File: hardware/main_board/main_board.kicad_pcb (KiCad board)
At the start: 4 copper layers, 155.2 x 50 mm, 179 parts, among them J1 USB_C_Receptacle_USB2.0_16P, J2 BAT1, J3 Conn_02x05_Odd_Even, J4 Conn_02x05_Odd_Even, Q1 FDMC4435BZ, Q10 MMBTA92, Q11 MMBTA92, Q12 MMBTA42, Q13 MMBTA42, Q14 MMBTA92, Q15 MMBTA92, Q16 MMBTA42, Q17 MMBTA42, Q18 MMBTA92, Q19 MMBTA92, Q2 MMBT3904, Q20 FDS2734, Q3 MMBT3904, Q4 MMBTA42, Q5 MMBTA42, Q6 MMBTA92, Q7 MMBTA92, Q8 MMBTA42, Q9 MMBTA42, SW1 PTS645VK31LFS, SW2 PTS645VK31LFS, SW3 PTS645VK31LFS, U1 SRV05-4, U10 TPS61022, U11 ESP32-S3-WROOM1, U12 TPS2121, U13 TPS22810DBVR, U14 74HC238, U15 LM5155, U16 BQ27441DRZR-G1A, U2 CP2102N-A02-GQFN28, U3 HUSB238_002DD, U4 TPS22918DBVR, U5 BQ25601, U6 DFPlayer_mini, U7 DS3231MZ, U8 TPS63802, U9 NCH2800HV

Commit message: WIP: update mainboard componemt LCSC PN
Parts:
- C28: value 120n -> 220n
- C29: value 50p -> 220p
- J2, LS1: footprint Connector_JST:JST_XH_S2B-XH-A_1x02_P2.50mm_Horizontal -> Connector_JST:JST_PH_B2B-PH-SM4-TB_1x02-1MP_P2.00mm_Vertical
- R74: value 22k -> 3.3k
- moved LS1 2.93 mm to (82.7, 125.9), turned to 0 degrees
- moved J2 2.02 mm to (193.7, 141.0), turned to 90 degrees
- moved C7 1.79 mm to (91.2, 129.8)
- moved C4 1.79 mm to (94.0, 124.4)
- moved U4 1.79 mm to (94.2, 129.9)
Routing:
- net DF_EN: track 5.15 -> 55.7 mm
- net Net-(U6-SPK_2): track 33.2 -> 28.5 mm
- net +5V: track 161.6 -> 159.1 mm
- net Net-(U6-SPK_1): track 21.3 -> 23.4 mm
- net Net-(U4-VOUT): track 20.3 -> 21.2 mm
- net VBAT: track 170.2 -> 169.3 mm, vias 4 -> 5
- net U1RXD: track 64.8 -> 64.1 mm

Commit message: WIP: mainboard schematic
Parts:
- moved J2 1.07 mm to (192.6, 141.2)
- moved C7 0.56 mm to (90.6, 129.7)
- moved C4 0.56 mm to (93.5, 124.2)
- moved U4 0.56 mm to (93.7, 129.8)
- moved LS1 0.50 mm to (83.1, 126.2)
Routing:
- net I2C0_SCL: track 104.3 -> 168.7 mm
- net I2C1_SDA: track 41.1 -> 76.6 mm
- net I2C1_SCL: track 40.0 -> 73.8 mm
- net I2C0_SDA: track 139.7 -> 171.6 mm
- net CHIP_PU: track 13.7 -> 37.0 mm, vias 1 -> 2
- net Net-(U13-VIN): track 10.3 -> 17.0 mm, vias 0 -> 1
- net VSYS: track 33.5 -> 39.8 mm
- net +5V: track 159.1 -> 164.7 mm
- net GND: track 89.0 -> 93.1 mm
- net DF_EN: track 55.7 -> 59.7 mm
- net BAT_LOW: track 88.2 -> 84.3 mm
- net +3V3: track 164.9 -> 162.5 mm, vias 5 -> 8
- net PGND1: track 24.5 -> 22.1 mm, vias 34 -> 37
- net Net-(Q12-B): track 0.00 -> 1.71 mm
- net VBAT: track 169.3 -> 167.8 mm
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
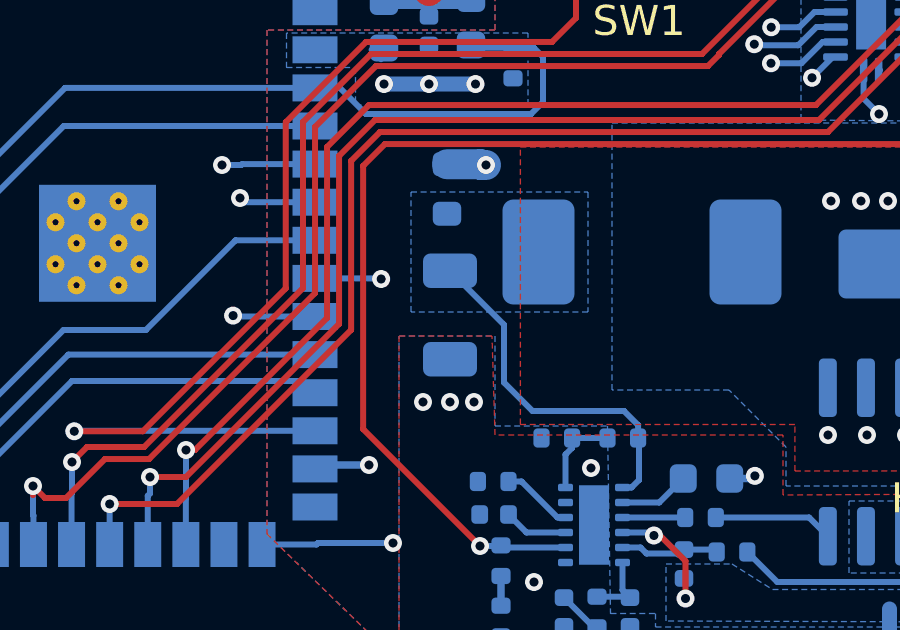
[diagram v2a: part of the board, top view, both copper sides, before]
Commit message: hw(main_board): update LCSC PN
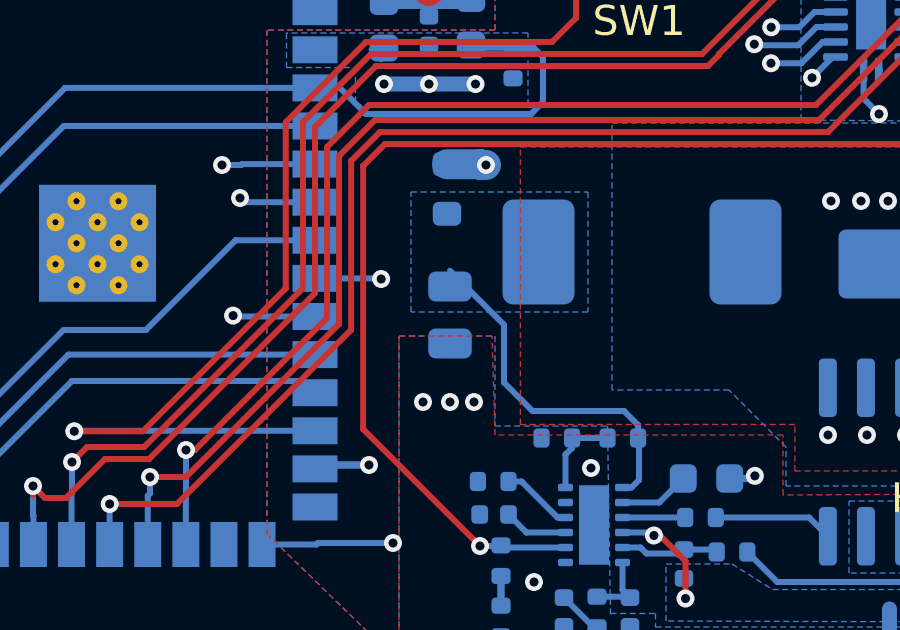
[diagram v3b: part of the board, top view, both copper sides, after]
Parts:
- C22: value 100nF -> 100n
- C25: value 100u -> 10u; footprint Capacitor_SMD:C_1206_3216Metric -> Capacitor_SMD:C_0805_2012Metric

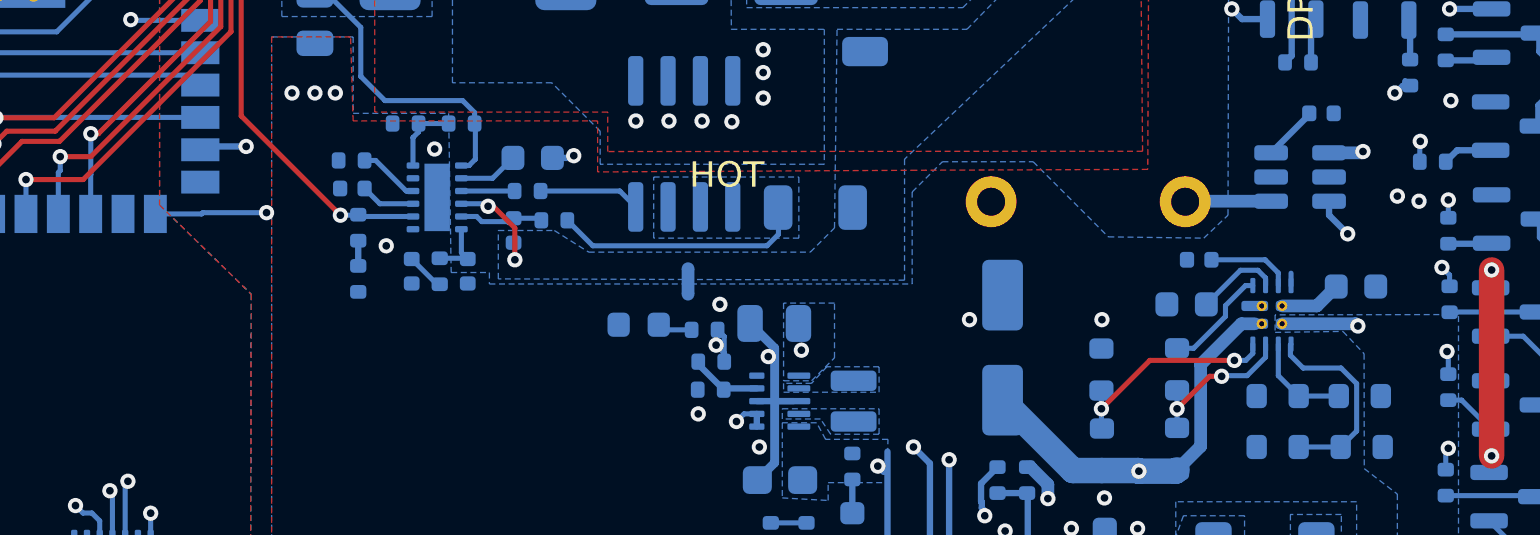
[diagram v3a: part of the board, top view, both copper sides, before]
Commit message: hw(sch): add input detect signal from TPS2121 to let ESP32 know which input is selected for HV power
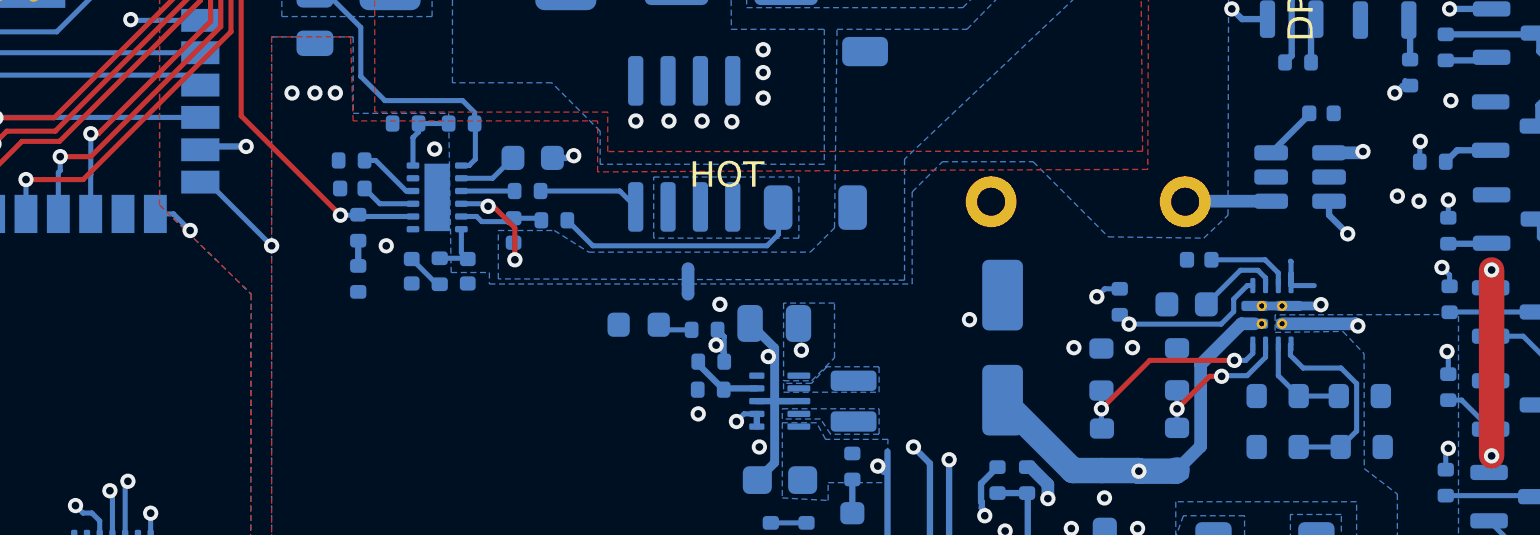
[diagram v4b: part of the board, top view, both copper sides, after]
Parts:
- removed C21: 1u, Capacitor_SMD:C_0603_1608Metric
- added R84: 10k, Resistor_SMD:R_0402_1005Metric, B.Cu at (171.3, 124.9)
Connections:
- U11 pad 14: unconnected-(U11-IO20-Pad14) -> VIN_ST
- U12 pad 9: PGND1 -> VIN_ST
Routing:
- net VIN_ST: track 0.00 -> 45.1 mm, vias 0 -> 2
- net +5V: track 164.7 -> 175.8 mm, vias 7 -> 8
- net PGND1: track 22.1 -> 19.7 mm, vias 37 -> 38
- net Net-(U13-VIN): track 17.0 -> 15.5 mm, vias 1 -> 2

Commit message: layout(main): adjust layout
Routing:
- net +5V: track 175.8 -> 174.5 mm
- net Net-(D4-A): vias 11 -> 23
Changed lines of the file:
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@@
 		(tags "RUX0012A Texas VQFN-HR NoLead")
 		(property "Reference" "U12"
-			(at -0.025 2.4125 0)
+			(at -3.225 1.4125 0)
 			(layer "B.SilkS")
 			(effects
@@
 		(tags "resistor")
 		(property "Reference" "R82"
-			(at 0.41 1.3 90)
+			(at 0.71 1.4 90)
 			(layer "B.SilkS")
 			(effects
@@
 		(tags "resistor")
 		(property "Reference" "R83"
-			(at 1.2 1.2 90)
+			(at 1.6 1.4 90)
 			(layer "B.SilkS")
 			(effects
@@
 		(tags "capacitor")
 		(property "Reference" "R36"
-			(at 2.95 0 0)
+			(at 1.925 1.8 0)
 			(layer "B.SilkS")
 			(effects
@@
 		(tags "capacitor")
 		(property "Reference" "C22"
-			(at 2.8 0.15 0)
+			(at -2.78 0.65 0)
 			(layer "B.SilkS")
 			(effects
@@
 		(tags "resistor")
 		(property "Reference" "R84"
-			(at 0 1.17 90)
+			(at 1.7 -2.1 0)
 			(layer "B.SilkS")
 			(effects
@@
 	)
 	(via
-		(at 97.425 124.375)
+		(at 98.2 124.375)
 		(size 0.6)
 		(drill 0.3)
@@
 	)
 	(segment
-		(start 96.0375 124.25)
-		(end 98.55 124.25)
-		(width 1)
-		(layer "B.Cu")
-		(net 20)
-	)
-	(segment
-		(start 97.3 124.25)
-		(end 97.425 124.375)
-		(width 1)
-		(layer "B.Cu")
-		(net 20)
-	)
-	(segment
 		(start 180.5625 125.7625)
 		(end 180.65 125.85)
@@
 	)
 	(segment
+		(start 96.1625 124.375)
+		(end 96.0375 124.25)
+		(width 0.75)
+		(layer "B.Cu")
+		(net 20)
+	)
+	(segment
+		(start 98.2 124.375)
+		(end 96.1625 124.375)
+		(width 0.75)
+		(layer "B.Cu")
+		(net 20)
+	)
+	(segment
 		(start 110.874 131.624)
 		(end 109.628021 131.624)
@@
 	)
 	(segment
+		(start 98.2 124.375)
+		(end 99.870958 124.375)
+		(width 1)
+		(layer "In1.Cu")
+		(net 20)
+	)
+	(segment
 		(start 179.901 123.801)
 		(end 180.65 124.55)
@@
 	)
 	(segment
-		(start 99.870958 124.375)
-		(end 97.425 124.375)
+		(start 180.65 124.55)
+		(end 180.65 125.85)
 		(width 1)
 		(layer "In1.Cu")
@@
 	)
 	(segment
-		(start 180.65 124.55)
-		(end 180.65 125.85)
+		(start 99.870958 124.375)
+		(end 108.4 132.904042)
 		(width 1)
 		(layer "In1.Cu")
@@
 	)
 	(segment
-		(start 108.4 132.904042)
-		(end 99.870958 124.375)
-		(width 1)
-		(layer "In1.Cu")
-		(net 20)
-	)
-	(segment
 		(start 170.3 118.4)
 		(end 174.5 118.4)
@@
 	)
 	(segment
-		(start 180.256083 126.801)
-		(end 180.4 126.801)
-		(width 0.5)
-		(layer "In1.Cu")
-		(net 28)
-	)
-	(segment
 		(start 181.601 126.243918)
 		(end 181.043918 126.801)
@@
 	)
 	(via
+		(at 151.4 110.6)
+		(size 0.6)
+		(drill 0.3)
+		(layers "F.Cu" "B.Cu")
+		(free yes)
+		(net 63)
+	)
+	(via
+		(at 147.7 112.5)
+		(size 0.6)
+		(drill 0.3)
+		(layers "F.Cu" "B.Cu")
+		(free yes)
+		(net 63)
+	)
+	(via
 		(at 153.4 110)
 		(size 0.6)
@@
 	)
 	(via
+		(at 152.3 114.6)
+		(size 0.6)
+		(drill 0.3)
+		(layers "F.Cu" "B.Cu")
+		(free yes)
+		(net 63)
+	)
+	(via
 		(at 154.9 117.8)
 		(size 0.6)
@@
 	)
 	(via
+		(at 151.4 112.4)
+		(size 0.6)
+		(drill 0.3)
+		(layers "F.Cu" "B.Cu")
+		(free yes)
+		(net 63)
+	)
+	(via
+		(at 151.4 111.5)
+		(size 0.6)
+		(drill 0.3)
+		(layers "F.Cu" "B.Cu")
+		(free yes)
+		(net 63)
+	)
+	(via
 		(at 157.3 115)
 		(size 0.6)
@@
 	)
 	(via
+		(at 147.7 111.6)
+		(size 0.6)
+		(drill 0.3)
+		(layers "F.Cu" "B.Cu")
+		(free yes)
+		(net 63)
+	)
+	(via
+		(at 153.6 114.6)
+		(size 0.6)
+		(drill 0.3)
+		(layers "F.Cu" "B.Cu")
+		(free yes)
+		(net 63)
+	)
+	(via
 		(at 152.4 110)
 		(size 0.6)
@@
 	)
 	(via
+		(at 154.9 114.6)
+		(size 0.6)
+		(drill 0.3)
+		(layers "F.Cu" "B.Cu")
+		(free yes)
+		(net 63)
+	)
+	(via
+		(at 151.4 113.4)
+		(size 0.6)
+		(drill 0.3)
+		(layers "F.Cu" "B.Cu")
+		(free yes)
+		(net 63)
+	)
+	(via
+		(at 147.7 113.5)
+		(size 0.6)
+		(drill 0.3)
+		(layers "F.Cu" "B.Cu")
+		(free yes)
+		(net 63)
+	)
+	(via
+		(at 147.7 110.7)
+		(size 0.6)
+		(drill 0.3)
+		(layers "F.Cu" "B.Cu")
+		(free yes)
+		(net 63)
+	)
+	(via
 		(at 152.3 117.8)
 		(size 0.6)
@@
 		(net 63)
 	)
+	(via
+		(at 156.1 114.6)
+		(size 0.6)
+		(drill 0.3)
+		(layers "F.Cu" "B.Cu")
+		(free yes)
+		(net 63)
+	)
 	(segment
 		(start 146.675 120.05)
@@
 	)
 	(segment
-		(start 162.32 108.2)
-		(end 165.4 108.2)
+		(start 164 108.2)
+		(end 165 107.2)
 		(width 0.2)
 		(layer "B.Cu")
@@
 	)
 	(segment
+		(start 165 104.6)
+		(end 165.3 104.3)
+		(width 0.2)
+		(layer "B.Cu")
+		(net 68)
+	)
+	(segment
 		(start 185.8 131.6)
 		(end 185.8 131.05)
@@
 	)
 	(segment
-		(start 166.43 107.17)
+		(start 165 107.2)
+		(end 165 104.6)
+		(width 0.2)
+		(layer "B.Cu")
+		(net 68)
+	)
+	(segment
+		(start 165.3 104.3)
 		(end 166.43 104.3)
 		(width 0.2)
@@
 	)
 	(segment
+		(start 162.32 108.2)
+		(end 164 108.2)
+		(width 0.2)
+		(layer "B.Cu")
+		(net 68)
+	)
+	(segment
 		(start 185.9 113.4)
 		(end 184.25 113.4)
@@
 	)
 	(segment
-		(start 165.4 108.2)
-		(end 166.43 107.17)
-		(width 0.2)
-		(layer "B.Cu")
-		(net 68)
-	)
-	(segment
 		(start 173.7 105.56)
 		(end 173.87 105.73)
@@
 				(xy 189.9 123.51) (xy 189.8 136.5) (xy 212.5 136.5) (xy 212.5 145.7) (xy 137.5 145.7) (xy 137.5 141.8)
 				(xy 138 141.8) (xy 138 114.5) (xy 141.2 114.5) (xy 141.2 117.5) (xy 144.95 117.5) (xy 145.05 123.75)
-				(xy 146.55 123.75) (xy 146.55 124.2) (xy 163.15 124.2) (xy 163.15 120.5875) (xy 164.3375 119.4)
+				(xy 146.55 123.75) (xy 146.55 124.2) (xy 163.8 124.05) (xy 163.85 120.5875) (xy 165.0375 119.4)
 				(xy 167.9 119.4) (xy 170.85 122.35) (xy 174.6 122.4) (xy 175.55 121.5) (xy 175.6 102.8) (xy 162.8 102.8)
 				(xy 162.8 107.4) (xy 151.4 107.3) (xy 151.4 96.7) (xy 190 96.8)
@@
 		(polygon
 			(pts
-				(xy 160.2 114.2) (xy 165.3 114.2) (xy 168 111.45) (xy 168 103.15) (xy 170.15 103.15) (xy 170.35 112.2)
-				(xy 162.85 119.3) (xy 162.85 124.05) (xy 146.9 124) (xy 146.9 122.1) (xy 149.1 122.1) (xy 150.45 122.95)
+				(xy 160.2 114.2) (xy 165.3 114.2) (xy 168 111.45) (xy 168 103.15) (xy 170.15 103.15) (xy 170.35 113.2)
+				(xy 162.85 120.3) (xy 162.85 124.05) (xy 146.9 124) (xy 146.9 122.1) (xy 149.1 122.1) (xy 150.45 122.95)
 				(xy 159.15 122.95) (xy 160.1 122)
 			)

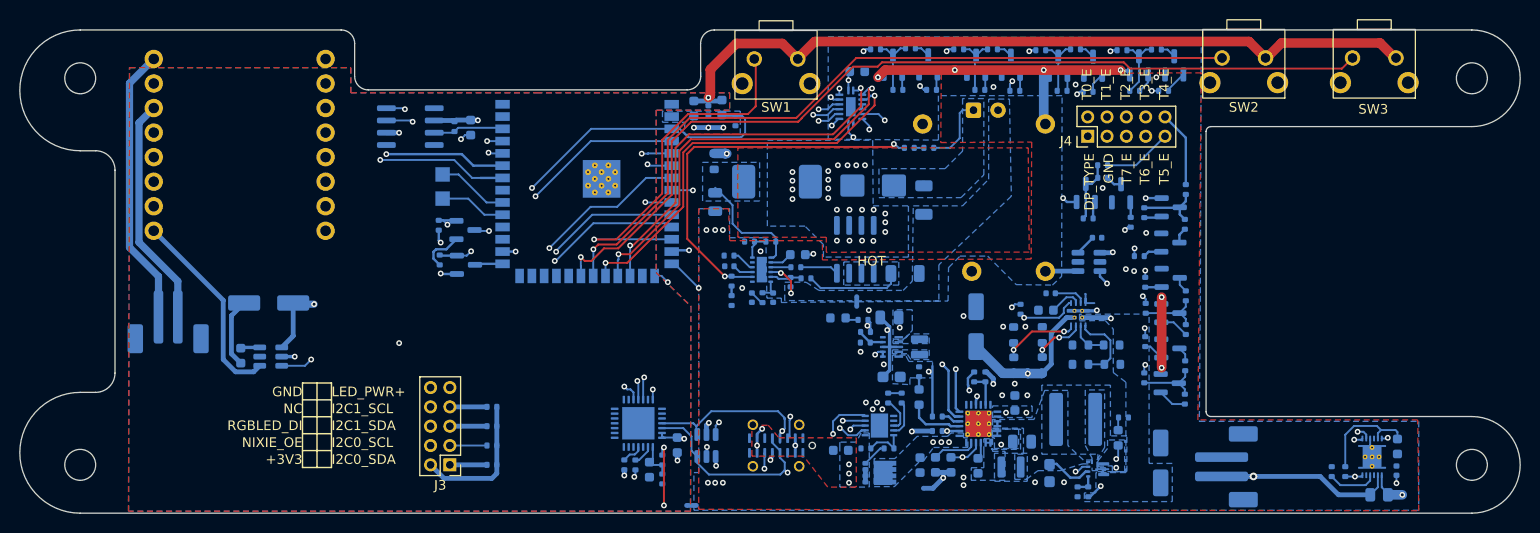
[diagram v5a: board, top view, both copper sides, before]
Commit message: layout(main): change battery and speaker connector footprint
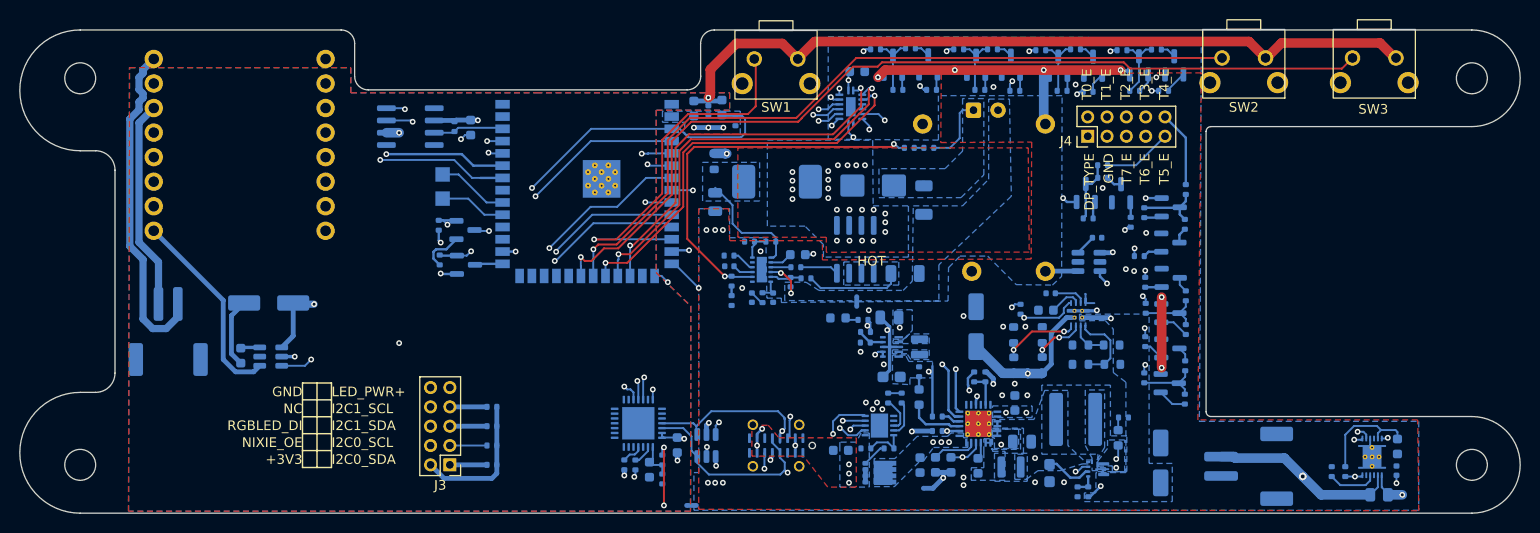
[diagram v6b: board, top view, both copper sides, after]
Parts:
- J2, LS1: footprint Connector_JST:JST_PH_B2B-PH-SM4-TB_1x02-1MP_P2.00mm_Vertical -> Connector_JST:JST_PH_S2B-PH-SM4-TB_1x02-1MP_P2.00mm_Horizontal
- moved J2 2.30 mm to (194.9, 141.2), turned to -90 degrees
- moved LS1 1.00 mm to (83.1, 127.2), turned to 180 degrees
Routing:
- net Net-(U6-SPK_2): track 29.0 -> 34.7 mm
- net Net-(U6-SPK_1): track 23.9 -> 21.7 mm
- net VBAT: track 167.8 -> 168.7 mm

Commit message: fix(hw): fix BQ25601 can not set 12V OVP after power reset. Due to BQ25601 will reset the register after power reset, HUSB238 need to ask 5V for the first stage, then use I2C to ask 12V PDO to makes the HV boost converter for better efficiency.
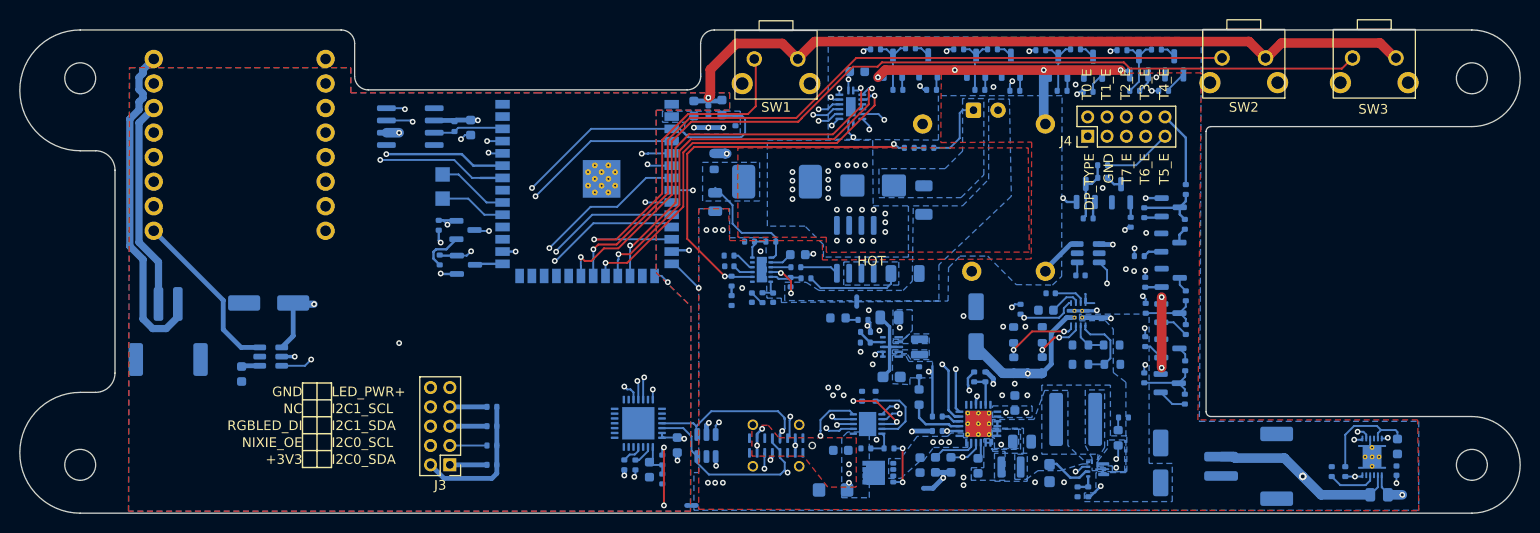
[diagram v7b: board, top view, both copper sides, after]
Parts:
- added D5: SMF28A, Diode_SMD:D_SMF, B.Cu at (151.9, 143.6)
- C27: value 100n -> 1u
- R20, R21, R22, R23: value 4.7k -> 1.3k
- R8: value 10k -> 0
- moved C23 4.26 mm to (177.5, 121.4)
- moved R6 2.71 mm to (156.3, 133.9)
- moved R8 2.71 mm to (154.9, 133.9)
- moved C7 1.90 mm to (90.7, 131.6)
- moved U3 1.24 mm to (155.5, 136.8)
- moved U13 0.90 mm to (178.3, 119.1)
- turned Q1 to 180 degrees
- turned R7 to 180 degrees
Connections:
- C24 pad 1: +5V -> +3V3
- C3 pad 1: Net-(Q1-S) -> Net-(D5-A1)
- J1 pad A4: Net-(Q1-S) -> Net-(D5-A1)
- J1 pad A9: Net-(Q1-S) -> Net-(D5-A1)
- J1 pad B4: Net-(Q1-S) -> Net-(D5-A1)
- J1 pad B9: Net-(Q1-S) -> Net-(D5-A1)
- Q1 pad 1: Net-(Q1-S) -> VBUS
- Q1 pad 5: VBUS -> Net-(D5-A1)
- R5 pad 1: Net-(Q1-S) -> Net-(D5-A1)
- R84 pad 2: +5V -> +3V3
- U1 pad 5: Net-(Q1-S) -> unconnected-(U1-VP-Pad5)
- U13 pad 4: HV_PWR+ -> Net-(U13-CT)
- U13 pad 6: Net-(U13-CT) -> HV_PWR+
- U14 pad 16: +5V -> +3V3
- U14 pad 6: +5V -> +3V3
- U3 pad 1: Net-(Q1-S) -> Net-(D5-A1)
- U3 pad 6: unconnected-(U3-SDA-Pad6) -> I2C0_SCL
- U3 pad 7: unconnected-(U3-SCL-Pad7) -> I2C0_SDA
- U4 pad 4: Net-(U4-VOUT) -> Net-(U4-CT)
- U4 pad 6: Net-(U4-CT) -> Net-(U4-VOUT)
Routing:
- net +5V: track 174.5 -> 119.9 mm, vias 8 -> 5
- net +3V3: track 162.5 -> 204.7 mm, vias 8 -> 11
- net I2C0_SDA: track 171.6 -> 185.1 mm, vias 3 -> 4
- net Net-(Q1-S): track 12.2 -> 0.00 mm, vias 7 -> 0
- net GND: track 93.1 -> 86.0 mm
- net Net-(D5-A1): track 0.00 -> 5.52 mm, vias 0 -> 6
- net Net-(U3-VSET): track 3.54 -> 7.94 mm, vias 0 -> 2
- net Net-(U3-ISET): track 3.71 -> 7.66 mm
- net I2C0_SCL: track 168.7 -> 172.6 mm, vias 3 -> 4
- net Net-(U4-VOUT): track 20.9 -> 17.7 mm
- net Net-(Q1-G): track 2.57 -> 5.41 mm, vias 0 -> 2
- net USB_D+: track 31.4 -> 29.9 mm
- net PGND1: track 19.7 -> 18.3 mm, vias 38 -> 39
- net Net-(J1-CC1): track 19.7 -> 18.4 mm
- net Net-(U3-GATE): track 4.28 -> 2.99 mm
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- added copper zone on B.Cu, net Net-(D5-A1)
- added copper zone on F.Cu, net Net-(D5-A1)
- removed copper zone on B.Cu, net Net-(Q1-S)
- removed copper zone on F.Cu, net Net-(Q1-S)
